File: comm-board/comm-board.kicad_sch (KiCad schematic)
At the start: 33 parts, among them J1 Step Down 5V, J4 ST-LINK, J5 Conn_01x02, J6 Power, J7 Communication, J9 Conn_01x02, U2 LF33_TO220, U3 STM32C011F4Px, Y1 Crystal

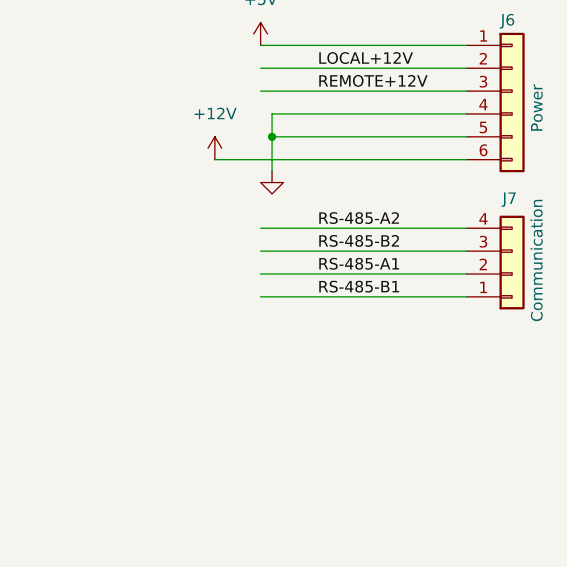
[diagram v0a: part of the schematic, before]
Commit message: PCB: comm: Cleanup and production configuration
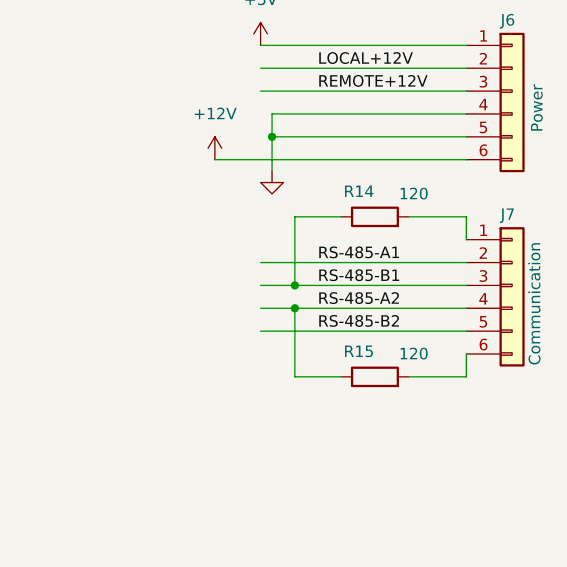
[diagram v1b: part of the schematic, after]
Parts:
- removed J7: Communication, _Footprints:PTSA-0.5-4-2.5-Z, symbol Connector_Generic:Conn_01x04
- added J7: Communication, _Footprints:PTSA-0.5-6-2.5-Z, symbol Connector_Generic:Conn_01x06
- added R14, R15: 120, Resistor_THT:R_Axial_DIN0207_L6.3mm_D2.5mm_P7.62mm_Horizontal, symbol Device:R
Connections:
- net RS-485-A1: now also J7.2 (Pin_2)
- net RS-485-A2: now also J7.4 (Pin_4), R15.1
- net RS-485-B1: now also J7.3 (Pin_3), R14.1
- net RS-485-B2: now also J7.5 (Pin_5)
- new net: J7.6 (Pin_6), R15.2
- new net: J7.1 (Pin_1), R14.2

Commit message: PCB: comm: Add stencil holder
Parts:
- added H5, H6, H7: Conn_01x01, _Footprints:stencil-holder, symbol Connector_Generic:Conn_01x01
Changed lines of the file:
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@@
+	)
+	(symbol
+		(lib_id "Connector_Generic:Conn_01x01")
+		(at 31.75 26.67 0)
+		(unit 1)
+		(exclude_from_sim no)
+		(in_bom yes)
+		(on_board yes)
+		(dnp no)
+		(fields_autoplaced yes)
+		(property "Reference" "H5"
+			(at 34.29 25.3999 0)
+			(effects
+				(font
+					(size 1.27 1.27)
+				)
+				(justify left)
+			)
+		)
+		(property "Value" "Conn_01x01"
+			(at 34.29 27.9399 0)
+			(effects
+				(font
+					(size 1.27 1.27)
+				)
+				(justify left)
+				(hide yes)
+			)
+		)
+		(property "Footprint" "_Footprints:stencil-holder"
+			(at 31.75 26.67 0)
+			(effects
+				(font
+					(size 1.27 1.27)
+				)
+				(hide yes)
+			)
+		)
+		(property "Datasheet" "~"
+			(at 31.75 26.67 0)
+			(effects
+				(font
+					(size 1.27 1.27)
+				)
+				(hide yes)
+			)
+		)
+		(property "Description" "Generic connector, single row, 01x01, script generated (kicad-library-utils/schlib/autogen/connector/)"
+			(at 31.75 26.67 0)
+			(effects
+				(font
+					(size 1.27 1.27)
+				)
+				(hide yes)
+			)
+		)
+		(pin "1"
+		)
+		(instances
+			(project "comm-board"
+				(path "/1eb66430-9d80-40b3-8abc-b6efed81f200"
+					(reference "H5")
+					(unit 1)
+				)
+			)
+		)
 	)
 	(symbol
@@
 	)
 	(symbol
+		(lib_id "Connector_Generic:Conn_01x01")
+		(at 31.75 30.48 0)
+		(unit 1)
+		(exclude_from_sim no)
+		(in_bom yes)
+		(on_board yes)
+		(dnp no)
+		(fields_autoplaced yes)
+		(property "Reference" "H6"
+			(at 34.29 29.2099 0)
+			(effects
+				(font
+					(size 1.27 1.27)
+				)
+				(justify left)
+			)
+		)
+		(property "Value" "Conn_01x01"
+			(at 34.29 31.7499 0)
+			(effects
+				(font
+					(size 1.27 1.27)
+				)
+				(justify left)
+				(hide yes)
+			)
+		)
+		(property "Footprint" "_Footprints:stencil-holder"
+			(at 31.75 30.48 0)
+			(effects
+				(font
+					(size 1.27 1.27)
+				)
+				(hide yes)
+			)
+		)
+		(property "Datasheet" "~"
+			(at 31.75 30.48 0)
+			(effects
+				(font
+					(size 1.27 1.27)
+				)
+				(hide yes)
+			)
+		)
+		(property "Description" "Generic connector, single row, 01x01, script generated (kicad-library-utils/schlib/autogen/connector/)"
+			(at 31.75 30.48 0)
+			(effects
+				(font
+					(size 1.27 1.27)
+				)
+				(hide yes)
+			)
+		)
+		(pin "1"
+		)
+		(instances
+			(project "comm-board"
+				(path "/1eb66430-9d80-40b3-8abc-b6efed81f200"
+					(reference "H6")
+					(unit 1)
+				)
+			)
+		)
+	)
+	(symbol
 		(lib_id "power:GND")
 		(at 172.72 147.32 0)
@@
 					(unit 1)
 				)
+			)
+		)
+	)
+	(symbol
+		(lib_id "Connector_Generic:Conn_01x01")
+		(at 31.75 34.29 0)
+		(unit 1)
+		(exclude_from_sim no)
+		(in_bom yes)
+		(on_board yes)
+		(dnp no)
+		(fields_autoplaced yes)
+		(property "Reference" "H7"
+			(at 34.29 33.0199 0)
+			(effects
+				(font
+					(size 1.27 1.27)
+				)
+				(justify left)
+			)
+		)
+		(property "Value" "Conn_01x01"
+			(at 34.29 35.5599 0)
+			(effects
+				(font
+					(size 1.27 1.27)
+				)
+				(justify left)
+				(hide yes)
+			)
+		)
+		(property "Footprint" "_Footprints:stencil-holder"
+			(at 31.75 34.29 0)
+			(effects
+				(font
+					(size 1.27 1.27)
+				)
+				(hide yes)
+			)
+		)
+		(property "Datasheet" "~"
+			(at 31.75 34.29 0)
+			(effects
+				(font
+					(size 1.27 1.27)
+				)
+				(hide yes)
+			)
+		)
+		(property "Description" "Generic connector, single row, 01x01, script generated (kicad-library-utils/schlib/autogen/connector/)"
+			(at 31.75 34.29 0)
+			(effects
+				(font
+					(size 1.27 1.27)
+				)
+				(hide yes)
+			)
+		)
+		(pin "1"
+		)
+		(instances
+			(project "comm-board"
+				(path "/1eb66430-9d80-40b3-8abc-b6efed81f200"
+					(reference "H7")
+					(unit 1)
+				)

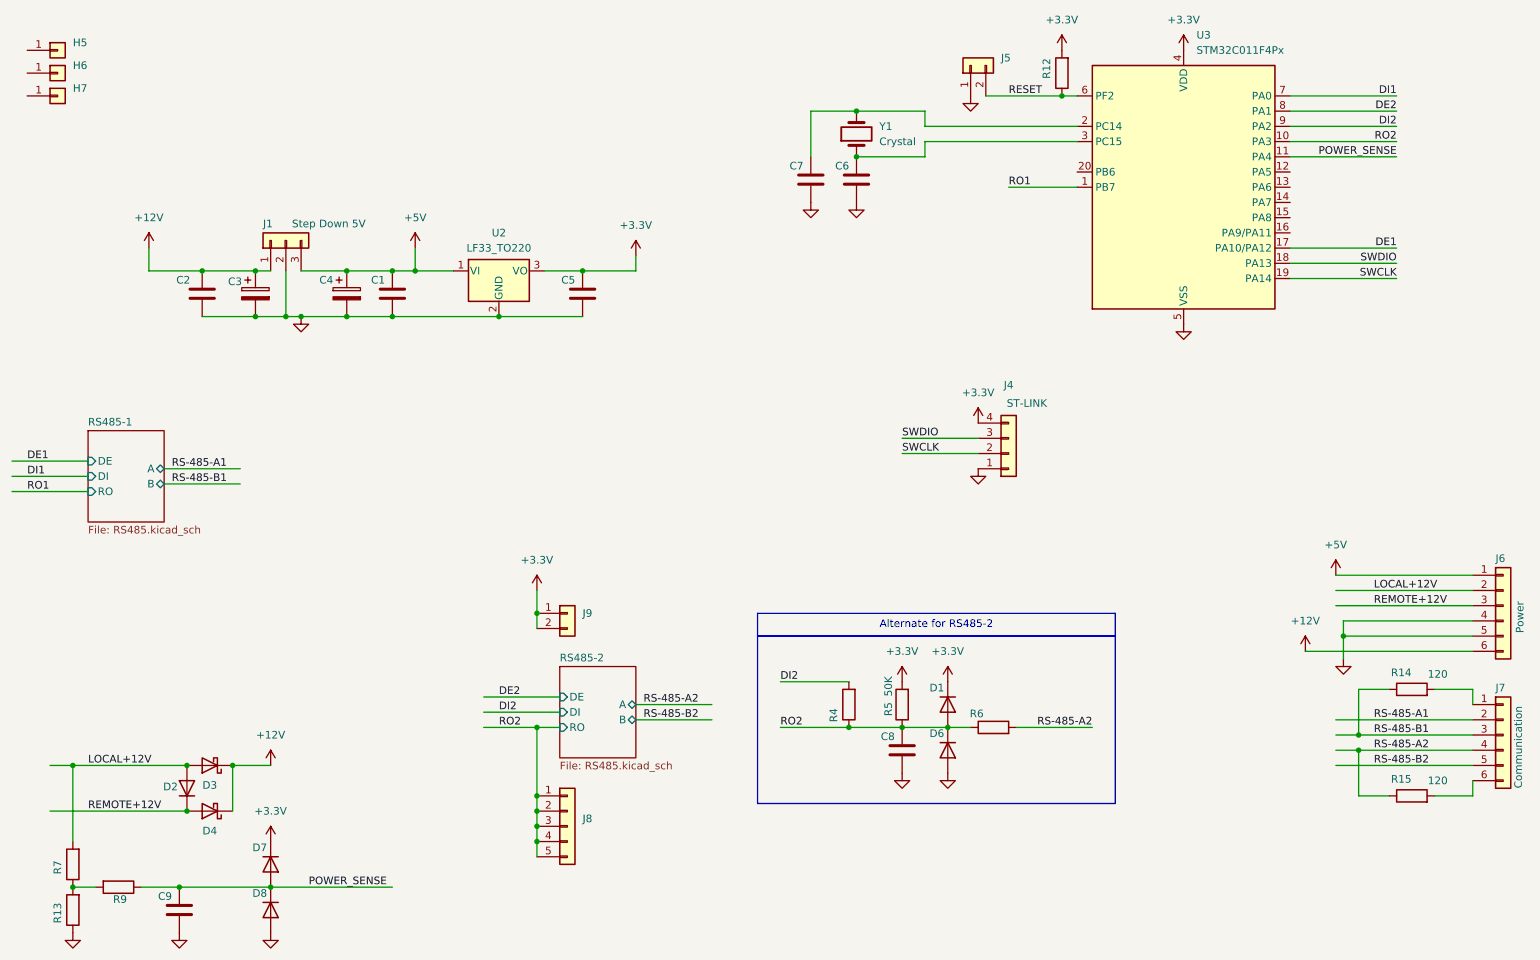
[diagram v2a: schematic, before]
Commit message: PCB: comm-board: component values and BOM
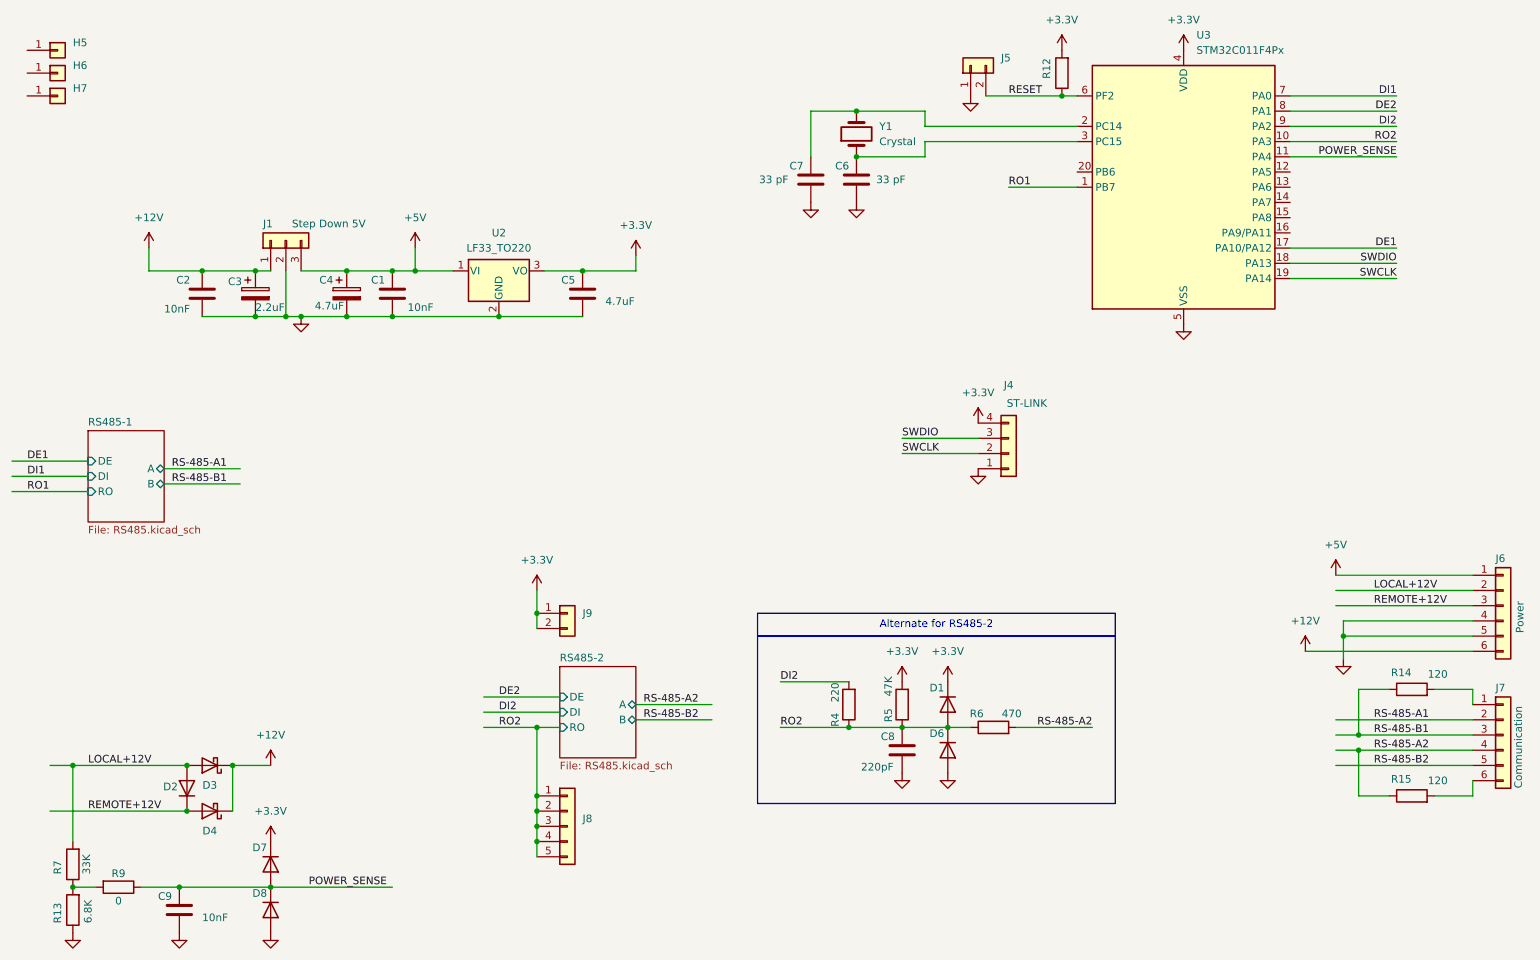
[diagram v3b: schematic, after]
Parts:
- C1, C2, C9: value ~ -> 10nF
- C3: value C_Polarized -> 2.2uF
- C4: value C_Polarized -> 4.7uF
- C5: value ~ -> 4.7uF
- C6, C7: value ~ -> 33 pF
- C8: value ~ -> 220pF
- R13: value 120 -> 6.8K
- R4: value 120 -> 220
- R5: value 50K -> 47K
- R6: value 120 -> 470
- R7: value 120 -> 33K
- R9: value 120 -> 0
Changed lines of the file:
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@@
 		(dnp no)
 		(property "Reference" "R4"
-			(at 161.29 137.668 90)
+			(at 161.544 138.43 90)
 			(effects
 				(font
@@
 			)
 		)
-		(property "Value" "120"
-			(at 161.544 132.842 90)
+		(property "Value" "220"
+			(at 161.544 133.858 90)
 			(effects
 				(font
 					(size 1.27 1.27)
 				)
-				(hide yes)
 			)
 		)
@@
 			)
 		)
-		(property "Value" "~"
+		(property "Value" "10nF"
 			(at 55.88 171.4499 0)
 			(effects
@@
 				)
 				(justify left)
-				(hide yes)
 			)
 		)
@@
 			)
 		)
-		(property "Value" "~"
-			(at 59.69 68.5799 0)
+		(property "Value" "10nF"
+			(at 49.53 69.85 0)
 			(effects
 				(font
@@
 				)
 				(justify left)
-				(hide yes)
 			)
 		)
@@
 			)
 		)
-		(property "Value" "C_Polarized"
-			(at 83.82 67.6909 0)
+		(property "Value" "4.7uF"
+			(at 74.676 69.342 0)
 			(effects
 				(font
@@
 				)
 				(justify left)
-				(hide yes)
 			)
 		)
@@
 			)
 		)
-		(property "Value" "120"
+		(property "Value" "470"
 			(at 191.008 137.414 90)
 			(effects
@@
 					(size 1.27 1.27)
 				)
-				(hide yes)
 			)
 		)
@@
 		(dnp no)
 		(property "Reference" "R5"
-			(at 170.434 136.652 90)
+			(at 170.434 137.668 90)
 			(effects
 				(font
@@
 			)
 		)
-		(property "Value" "50K"
+		(property "Value" "47K"
 			(at 170.434 132.842 90)
 			(effects
@@
 			)
 		)
-		(property "Value" "120"
-			(at 32.004 159.512 90)
+		(property "Value" "33K"
+			(at 36.576 162.56 90)
 			(effects
 				(font
 					(size 1.27 1.27)
 				)
-				(hide yes)
 			)
 		)
@@
 			)
 		)
-		(property "Value" "120"
-			(at 32.004 167.132 90)
+		(property "Value" "6.8K"
+			(at 36.83 170.434 90)
 			(effects
 				(font
 					(size 1.27 1.27)
 				)
-				(hide yes)
 			)
 		)
@@
 			)
 		)
-		(property "Value" "~"
-			(at 176.53 144.7799 0)
+		(property "Value" "220pF"
+			(at 165.862 146.304 0)
 			(effects
 				(font
@@
 				)
 				(justify left)
-				(hide yes)
 			)
 		)
@@
 			)
 		)
-		(property "Value" "C_Polarized"
-			(at 68.58 67.6909 0)
+		(property "Value" "2.2uF"
+			(at 64.77 69.596 0)
 			(effects
 				(font
@@
 				)
 				(justify left)
-				(hide yes)
 			)
 		)
@@
 			)
 		)
-		(property "Value" "~"
+		(property "Value" "4.7uF"
 			(at 123.19 68.5799 0)
 			(effects
@@
 				)
 				(justify left)
-				(hide yes)
 			)
 		)
@@
 			)
 		)
-		(property "Value" "~"
-			(at 168.91 49.5299 0)
+		(property "Value" "33 pF"
+			(at 168.402 48.26 0)
 			(effects
 				(font
@@
 				)
 				(justify left)
-				(hide yes)
 			)
 		)
@@
 		(dnp no)
 		(property "Reference" "R9"
-			(at 42.164 168.402 90)
+			(at 41.91 164.084 90)
 			(effects
 				(font
@@
 			)
 		)
-		(property "Value" "120"
-			(at 38.862 168.656 90)
+		(property "Value" "0"
+			(at 41.91 168.656 90)
 			(effects
 				(font
 					(size 1.27 1.27)
 				)
-				(hide yes)
 			)
 		)
@@
 			)
 		)
-		(property "Value" "~"
-			(at 161.29 49.5299 0)
+		(property "Value" "33 pF"
+			(at 148.844 48.26 0)
 			(effects
 				(font
@@
 				)
 				(justify left)
-				(hide yes)
 			)
 		)
@@
 			)
 		)
-		(property "Value" "~"
-			(at 91.44 68.5799 0)
+		(property "Value" "10nF"
+			(at 90.17 69.596 0)
 			(effects
 				(font
@@
 				)
 				(justify left)
-				(hide yes)
 			)
 		)
